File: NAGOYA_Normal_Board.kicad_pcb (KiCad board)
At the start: 2 copper layers, 94 parts, among them CN1 XT30-M, CN13 value, CN14 RefereeSystem, CN15 micro_B, J1 debug, J10 CAN3, J11 CAN3, J12 CAN3, J13 CAN3, J14 CAN3, J15 CAN3, J16 CAN3, J5 CAN3, J6 CAN3, J7 CAN3, J8 CAN3, J9 CAN3, Q2 DDTC114EUA-7-F, U1 Teensy4.1, U10 AP63357, U2 TCAN1042HVDR, U3 TCAN1042HVDR, U4 TCAN1042HVDR, U5 FT234XD, U6 TLP172AM, U7 BNO055, U9 LXES11DAA2-137, Y2 32.768 k

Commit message: PCBwo
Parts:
- removed C15: 47p, Capacitor_SMD:C_0402_1005Metric
- removed C16, C17: 22u, Resistor_SMD:R_1206_3216Metric
- removed D1: LED, LED_SMD:LED_0603_1608Metric
- removed J11, J12, J15, J16: CAN3, Connector_JST:JST_GH_SM02B-GHS-TB_1x02-1MP_P1.25mm_Horizontal
- removed L1: 6.8u, Inductor_SMD:L_TracoPower_TCK-047_5.2x5.8mm
- removed R1: 3.3k, Resistor_SMD:R_0603_1608Metric
- removed R14: 41.2k, Resistor_SMD:R_0201_0603Metric
- removed U10: AP63357, 0_PCB:V-DFN3020-13
- removed ZD12: ESD5Z7.0T1G, Diode_SMD:D_SOD-523
- added CN2: XT30-M, 0_PCB:AMASS_XT30U-M_1x02_P5.0mm_Vertical, F.Cu at (158.8, 90.5)
- added CN3: XT30-F, 0_PCB:AMASS_XT30U-F_1x02_P5.0mm_Vertical, F.Cu at (158.9, 84.0)
- added CN4: XT30-F, 0_PCB:AMASS_XT30U-F_1x02_P5.0mm_Vertical, F.Cu at (158.8, 77.7)
- added CN5: XT30-F, 0_PCB:AMASS_XT30U-F_1x02_P5.0mm_Vertical, F.Cu at (158.9, 71.3)
- added CN6: XT30-F, 0_PCB:AMASS_XT30U-F_1x02_P5.0mm_Vertical, F.Cu at (158.8, 65.0)
- added D6: LED, LED_SMD:LED_0603_1608Metric, F.Cu at (121.4, 123.8)
- added M78AR05-0.5: ~, 0_PCB:SIP3_LMS78-12_GAP, F.Cu at (120.5, 111.6)
- added R5: 3.3k, Resistor_SMD:R_0603_1608Metric, F.Cu at (123.7, 123.0)
- C14: value 0.1u(50V) -> 100uF; footprint Capacitor_SMD:C_0402_1005Metric -> Capacitor_SMD:CP_Elec_6.3x7.7
- CN1: footprint 0_PCB:AMASS_XT30PW-M_1x02_P2.50mm_Horizontal -> 0_PCB:AMASS_XT30U-M_1x02_P5.0mm_Vertical
- R12: value 22k -> 4.7k
- R13: value 220k -> 4.7k; footprint Resistor_SMD:R_0201_0603Metric -> Resistor_SMD:R_0805_2012Metric
- moved U1 232.1 mm to (147.6, 121.4), turned to 180 degrees
- moved J9 215.7 mm to (166.5, 114.5), turned to 90 degrees
- moved H4 214.1 mm to (167.0, 122.0)
- moved J10 210.1 mm to (166.5, 107.4), turned to 90 degrees
- moved H2 205.3 mm to (167.0, 58.0)
- moved C11 203.5 mm to (160.3, 121.8)
- moved C9 203.5 mm to (160.9, 113.1)
- moved D3 203.2 mm to (156.8, 122.4), turned to -90 degrees
- moved D4 201.1 mm to (157.6, 113.2), turned to -90 degrees
- moved C8 200.7 mm to (153.4, 121.6)
- moved J13 199.9 mm to (166.5, 99.9), turned to 90 degrees
- moved J14 195.3 mm to (166.5, 92.8), turned to 90 degrees
- moved C10 193.8 mm to (151.7, 113.5), turned to 180 degrees
- moved CN13 190.2 mm to (154.1, 103.6), turned to 90 degrees
- moved U3 187.3 mm to (153.0, 117.6)
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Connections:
- C13 pad 1: V_BATT -> +5V
- C14 pad 1: Net-(U10-BST) -> +5V
- C14 pad 2: Net-(C14-Pad2) -> GND
- J1 pad 3: RX6 -> RX8
- J1 pad 4: TX6 -> TX8
- J10 pad 1: CAN1_L -> CAN2_L
- J10 pad 2: CAN1_H -> CAN2_H
- J13 pad 1: CAN1_L -> CAN3_L
- J13 pad 2: CAN1_H -> CAN3_H
- J14 pad 1: CAN1_L -> CAN3_L
- J14 pad 2: CAN1_H -> CAN3_H
- J9 pad 1: CAN1_L -> CAN2_L
- J9 pad 2: CAN1_H -> CAN2_H
- JP2 pad 1: VCC -> +3.3V
- JP3 pad 1: VCC -> +3.3V
- R12 pad 1: V_BATT -> +3.3V
- R12 pad 2: GND -> IMU_SCL
- R13 pad 1: +5V -> +3.3V
- R13 pad 2: Net-(U10-FB) -> IMU_SDA
- R3 pad 1: CAN1_L -> CAN2_L
- R3 pad 2: CAN1_H -> CAN2_H
- R4 pad 1: CAN1_L -> CAN3_L
- R4 pad 2: CAN1_H -> CAN3_H
- U3 pad 6: CAN1_L -> CAN2_L
- U3 pad 7: CAN1_H -> CAN2_H
- U4 pad 6: CAN1_L -> CAN3_L
- U4 pad 7: CAN1_H -> CAN3_H
- ZD4 pad 1: CAN1_H -> CAN2_H
- ZD4 pad 2: CAN1_L -> CAN2_L
- ZD5 pad 1: CAN1_H -> CAN3_H
- ZD5 pad 2: CAN1_L -> CAN3_L
- ZD8 pad 1: TX6 -> TX8
- ZD9 pad 1: RX6 -> RX8
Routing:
- net +5V: track 0.00 -> 142.8 mm, vias 0 -> 6
- net +3.3V: track 0.00 -> 118.7 mm, vias 0 -> 7
- net CAN1_L: track 0.00 -> 52.6 mm, vias 0 -> 4
- net IMU_SDA: track 0.00 -> 52.5 mm, vias 0 -> 2
- net IMU_SCL: track 0.00 -> 51.8 mm, vias 0 -> 2
- net CAN_RX3: track 0.00 -> 50.7 mm, vias 0 -> 1
- net CAN_TX3: track 0.00 -> 48.4 mm, vias 0 -> 1
- net CAN1_H: track 0.00 -> 47.1 mm, vias 0 -> 4
- net CAN_RX1: track 0.00 -> 27.6 mm, vias 0 -> 2
- net CAN3_L: track 0.00 -> 26.9 mm
- net CAN_TX1: track 0.00 -> 26.6 mm, vias 0 -> 1
- net CAN3_H: track 0.00 -> 26.1 mm
- net RX3: track 0.00 -> 24.9 mm, vias 0 -> 2
- net TX3: track 0.00 -> 23.4 mm, vias 0 -> 2
- net Controller_RX: track 0.00 -> 22.8 mm
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- added copper zone on B.Cu, net Ammo_GND
- added copper zone on F.Cu, net Ammo_GND
- added copper zone on B.Cu, net GND
- added copper zone on F.Cu, net GND
- added copper zone on B.Cu, net V_Ammo
- added copper zone on F.Cu, net V_Ammo
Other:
- board outline added: 60 x 70 mm

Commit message: Update
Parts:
- added D10: LED, LED_SMD:LED_0603_1608Metric, F.Cu at (125.4, 80.5)
- added D8: LED, LED_SMD:LED_0603_1608Metric, F.Cu at (125.3, 76.8)
- added D9: LED, LED_SMD:LED_0603_1608Metric, F.Cu at (125.4, 78.8)
- added G***: LOGO, LOGO, F.Cu at (159.4, 58.6)
- added G***: LOGO, LOGO, F.Cu at (143.2, 118.0)
- added G***: LOGO, LOGO, F.Cu at (140.6, 85.4)
- added Q4: DDTC114EUA-7-F, Package_TO_SOT_SMD:SOT-323_SC-70, F.Cu at (129.0, 76.2)
- added Q5: DDTC114EUA-7-F, Package_TO_SOT_SMD:SOT-323_SC-70, F.Cu at (129.0, 78.8)
- added Q6: DDTC114EUA-7-F, Package_TO_SOT_SMD:SOT-323_SC-70, F.Cu at (129.0, 81.3)
- added R14: 3.3k, Resistor_SMD:R_0603_1608Metric, F.Cu at (122.0, 78.7)
- added R16: 3.3k, Resistor_SMD:R_0603_1608Metric, F.Cu at (122.1, 80.5)
- added R7: 3.3k, Resistor_SMD:R_0603_1608Metric, F.Cu at (122.1, 76.8)
- moved C7 10.5 mm to (119.1, 89.3), turned to 180 degrees
- moved R2 9.69 mm to (118.0, 85.4), turned to -90 degrees
- moved C6 7.99 mm to (125.0, 91.5), turned to -90 degrees
- moved D2 7.70 mm to (122.3, 89.2)
- moved ZD3 4.91 mm to (121.2, 85.3), turned to 180 degrees
- moved U2 3.96 mm to (127.0, 85.3), turned to 180 degrees
- moved CN3 3.50 mm to (162.4, 84.0)
- moved CN4 3.50 mm to (162.3, 77.7)
- moved CN5 3.50 mm to (162.4, 71.3)
- moved CN6 3.50 mm to (162.3, 65.0)
- moved C1 2.19 mm to (145.0, 84.0), turned to -90 degrees
- moved R13 1.39 mm to (138.3, 100.0)
- moved C4 1.29 mm to (122.8, 96.7)
- moved H2 1.00 mm to (167.0, 57.0)
- moved H3 1.00 mm to (113.0, 57.0)
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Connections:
- C22 pad 2: GNDA -> GND
- C23 pad 1: GNDA -> GND
- C24 pad 1: GNDA -> GND
- C26 pad 2: GNDA -> Net-(ZD11-A)
- JP1 pad 2: GNDA -> GND
- R48 pad 1: GNDA -> GND
- R49 pad 1: GNDA -> GND
- U1 pad 30: unconnected-(U1-38-Pad30) -> LED2
- U1 pad 31: unconnected-(U1-39-Pad31) -> LED3
- U1 pad 32: unconnected-(U1-40-Pad32) -> LED4
- U7 pad 15: GNDA -> GND
- U7 pad 16: GNDA -> GND
- U7 pad 17: GNDA -> GND
- U7 pad 2: GNDA -> GND
- U7 pad 25: GNDA -> GND
- ZD11 pad 2: GNDA -> Net-(ZD11-A)
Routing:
- net +3.3V: track 118.7 -> 188.4 mm, vias 7 -> 10
- net +5V: track 142.8 -> 186.2 mm, vias 6 -> 4
- net CAN1_L: track 52.6 -> 31.1 mm, vias 4 -> 2
- net GND: track 5.19 -> 17.8 mm, vias 3 -> 5
- net CAN1_H: track 47.1 -> 38.4 mm, vias 4 -> 0
- net CAN_RX1: track 27.6 -> 35.7 mm, vias 2 -> 1
- net /Vio: track 14.2 -> 21.0 mm
- net Net-(U5-3V3OUT): track 1.44 -> 5.50 mm, vias 0 -> 1
- net UART4_RX: track 4.00 -> 0.58 mm
- net UART4_TX: track 4.02 -> 0.65 mm, vias 1 -> 0
- net LED4: track 0.00 -> 2.90 mm
- net LED3: track 0.00 -> 2.87 mm
- net LED2: track 0.00 -> 2.85 mm
- net CAN_TX1: track 26.6 -> 29.1 mm
- net Net-(D10-K): track 0.00 -> 2.15 mm
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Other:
- board size 60 x 70 mm -> 60 x 71 mm

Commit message: recommit
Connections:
- C11 pad 1: /Vio -> Net-(D4-K)
- C7 pad 1: /Vio -> Net-(D2-K)
- C9 pad 1: /Vio -> Net-(D3-K)
- D2 pad 1: /Vio -> Net-(D2-K)
- D3 pad 1: /Vio -> Net-(D3-K)
- D4 pad 1: /Vio -> Net-(D4-K)
- U2 pad 5: /Vio -> Net-(D2-K)
- U3 pad 5: /Vio -> Net-(D3-K)
- U4 pad 5: /Vio -> Net-(D4-K)
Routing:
- net /Vio: track 21.0 -> 0.00 mm
- net Net-(D2-K): track 0.00 -> 11.5 mm
- net (no net): track 0.00 -> 9.50 mm

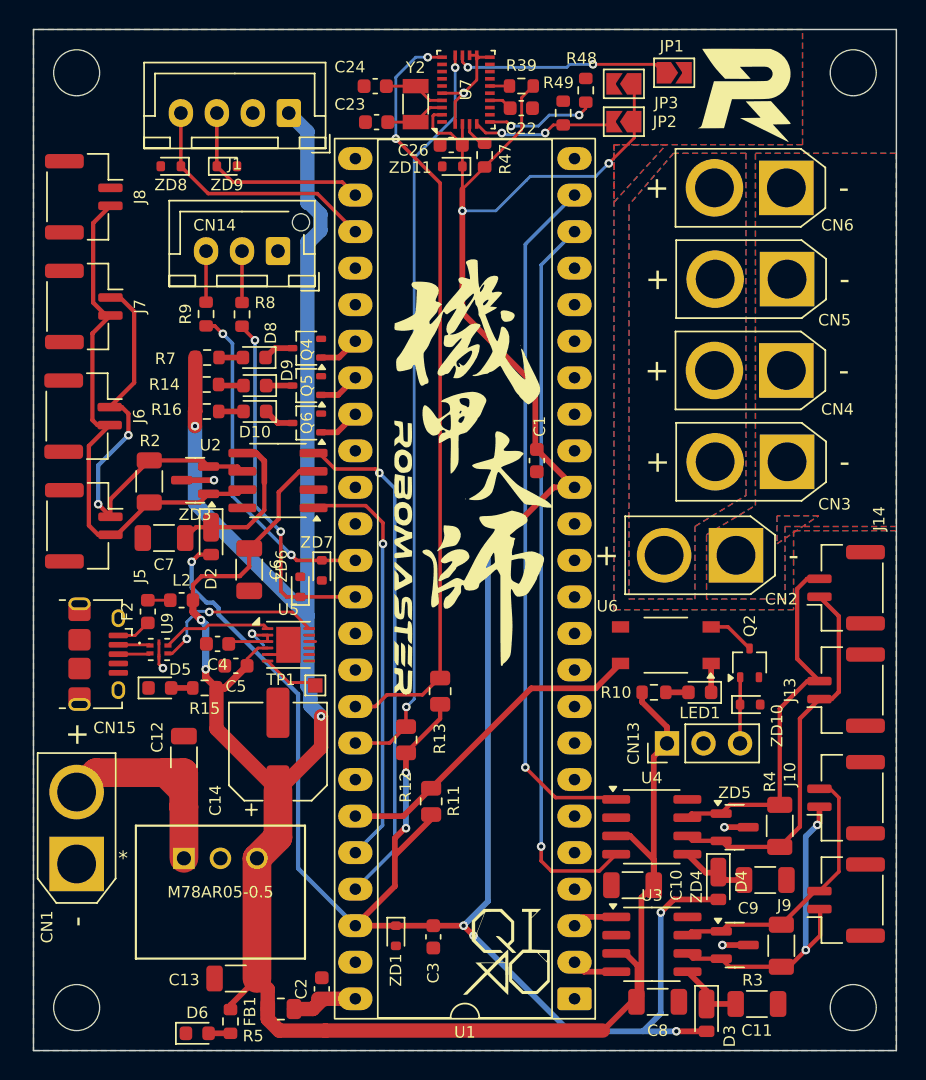
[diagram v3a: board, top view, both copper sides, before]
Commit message: USBシリアルを絶縁＞パターン変更
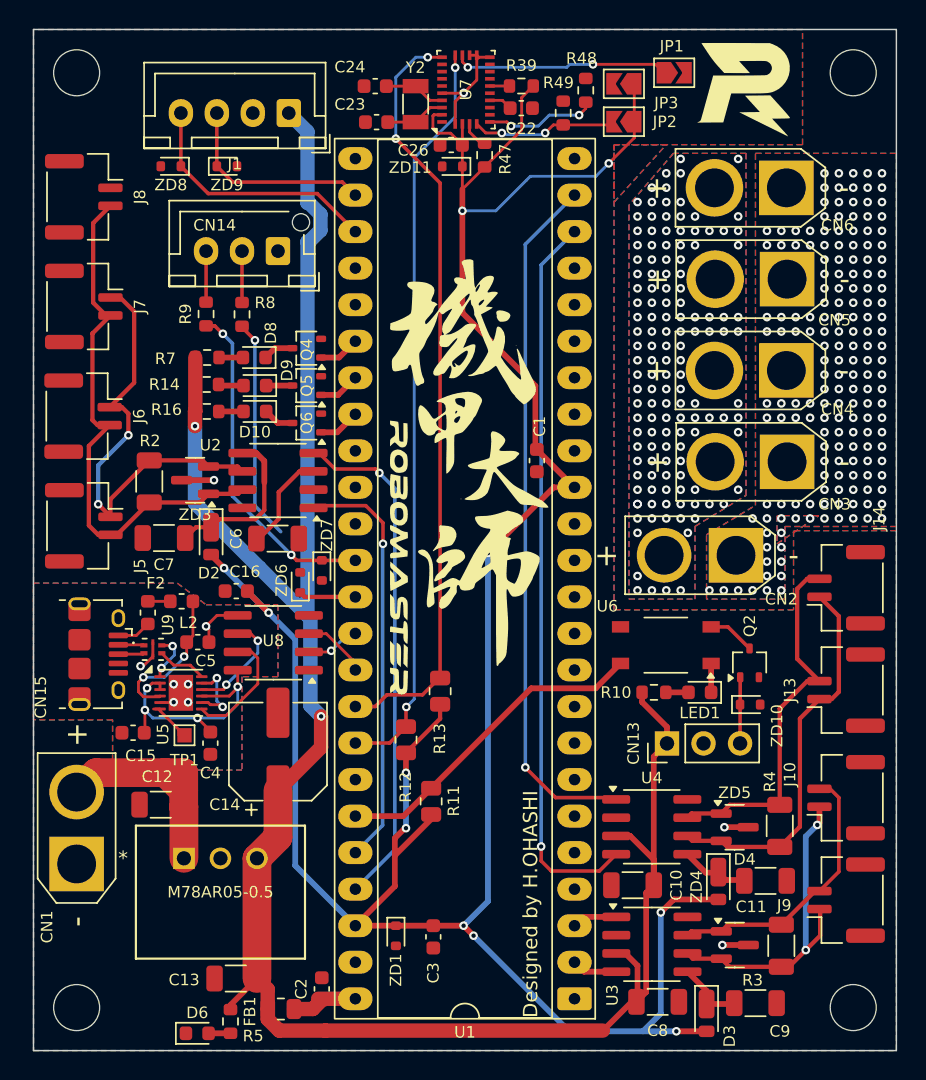
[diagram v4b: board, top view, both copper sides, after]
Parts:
- removed D5: LED, LED_SMD:LED_0603_1608Metric
- removed the G*** at (143.2, 118.0)
- removed R15: 1k, Resistor_SMD:R_0603_1608Metric
- added C15: 0.1u, Capacitor_SMD:C_0603_1608Metric, F.Cu at (116.9, 102.9)
- added C16: 0.1u, Capacitor_SMD:C_0603_1608Metric, F.Cu at (124.1, 93.0)
- added U8: ADuM121N, Package_SO:SOIC-8_3.9x4.9mm_P1.27mm, F.Cu at (126.7, 96.6)
- moved TP1 9.74 mm to (120.5, 103.1)
- moved C9 8.59 mm to (160.2, 121.7)
- moved C11 8.58 mm to (160.9, 113.2)
- moved U5 8.19 mm to (120.2, 100.1)
- moved C4 6.92 mm to (122.3, 103.6), turned to -90 degrees
- moved C12 3.66 mm to (118.8, 107.9), turned to 180 degrees
- moved C5 3.12 mm to (121.4, 96.6), turned to 0 degrees
- moved C6 2.93 mm to (127.0, 89.4), turned to 0 degrees
- moved U9 0.43 mm to (118.3, 97.1)
- moved G*** 0.40 mm to (159.3, 58.2)
- moved ZD6 0.31 mm to (128.6, 92.4)
- moved G*** 0.30 mm to (140.3, 85.4)
- moved F2 0.08 mm to (118.0, 94.5)
- moved L2 0.08 mm to (120.3, 93.8)
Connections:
- C4 pad 2: GND -> GNDREF
- C5 pad 1: +5V -> Net-(U5-VCC)
- C5 pad 2: GND -> GNDREF
- CN15 pad 5: GND -> GNDREF
- CN15 pad 6: GND -> GNDREF
- L2 pad 1: +5V -> Net-(U5-VCC)
- U5 pad 10: UART4_TX -> Net-(U5-RXD/D1)
- U5 pad 13: GND -> GNDREF
- U5 pad 4: +5V -> Net-(U5-VCC)
- U5 pad 5: GND -> GNDREF
- U5 pad 7: UART4_RX -> Net-(U5-TXD/D0)
- U9 pad 3: GND -> GNDREF
- U9 pad 6: GND -> GNDREF
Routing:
- net +5V: track 186.2 -> 157.8 mm, vias 4 -> 2
- net Net-(U5-3V3OUT): track 5.50 -> 18.3 mm, vias 1 -> 4
- net Net-(U5-VCC): track 0.00 -> 10.4 mm, vias 0 -> 2
- net (no net): track 9.50 -> 0.00 mm
- net Net-(U5-USBDP): track 12.2 -> 3.45 mm, vias 2 -> 0
- net Net-(U5-TXD/D0): track 0.00 -> 8.37 mm
- net GNDREF: track 0.00 -> 7.56 mm, vias 0 -> 6
- net Net-(U5-RXD/D1): track 0.00 -> 7.50 mm, vias 0 -> 2
- net RX3: track 24.9 -> 19.4 mm, vias 2 -> 1
- net Net-(U5-~{CTS}/D3): track 0.00 -> 4.95 mm, vias 0 -> 2
- net Net-(D3-K): track 0.00 -> 4.82 mm
- net Net-(D4-K): track 0.00 -> 4.68 mm
- net UART4_RX: track 0.58 -> 5.00 mm, vias 0 -> 1
- net Net-(U5-USBDM): track 7.62 -> 3.36 mm, vias 0 -> 2
- net UART4_TX: track 0.65 -> 4.77 mm
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- added copper zone on B.Cu, net GNDREF
- added copper zone on F.Cu, net GNDREF
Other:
- board text added: "Designed by H.OHASHI"

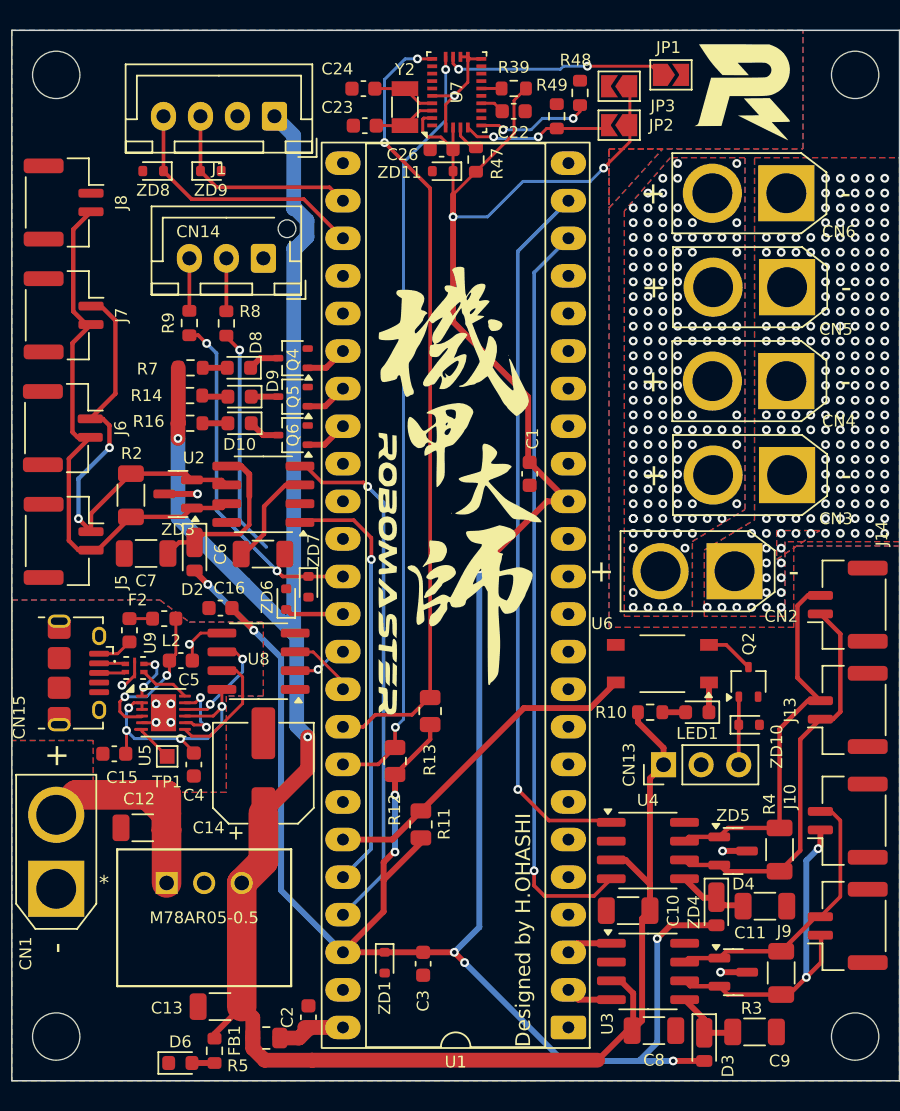
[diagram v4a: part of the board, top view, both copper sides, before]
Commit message: USBシリアルを絶縁
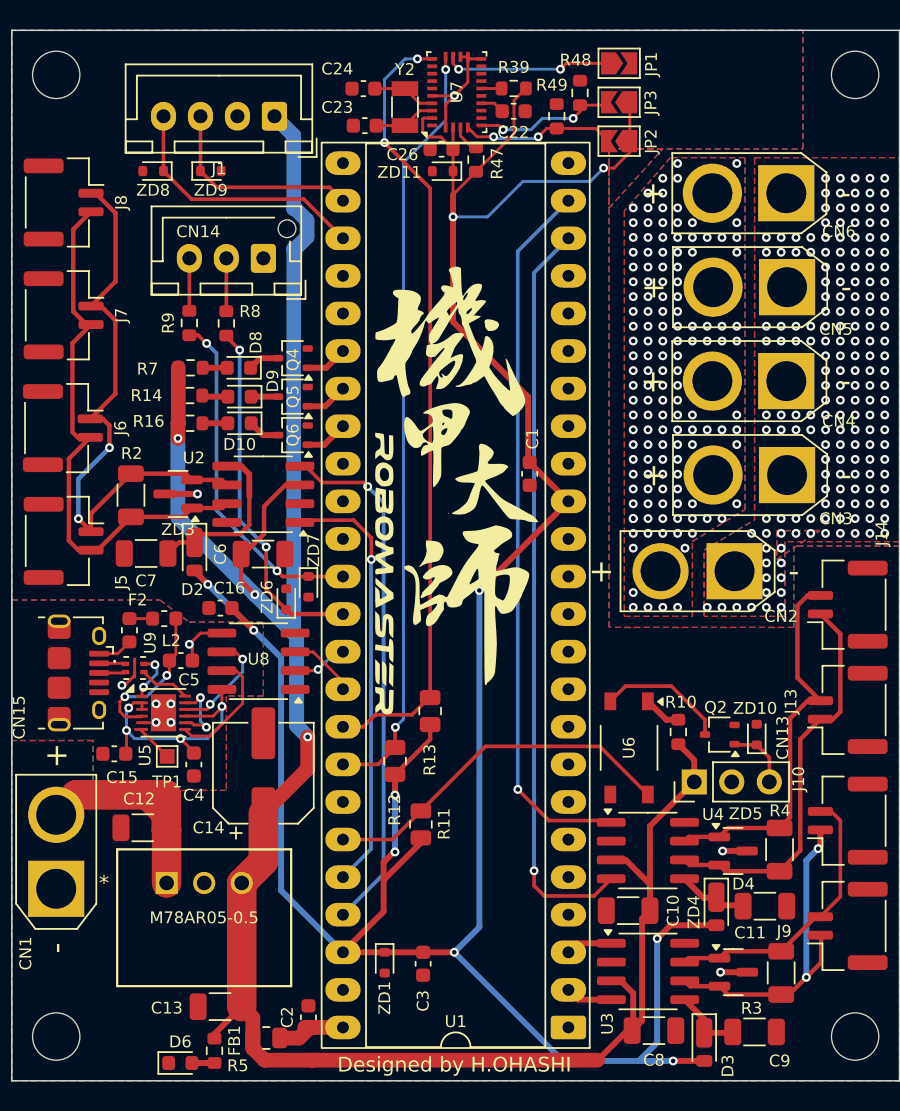
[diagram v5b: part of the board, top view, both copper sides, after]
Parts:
- removed the G*** at (159.3, 58.2)
- removed LED1: RED, LED_SMD:LED_0603_1608Metric
- moved U6 6.12 mm to (151.7, 102.5), turned to -90 degrees
- moved Q2 4.05 mm to (157.8, 101.6), turned to 180 degrees
- moved JP1 3.59 mm to (151.1, 56.2)
- moved CN13 2.37 mm to (156.1, 104.8)
- moved R10 2.33 mm to (155.1, 101.4), turned to 90 degrees
- moved JP2 1.08 mm to (151.0, 61.5)
- moved JP3 1.08 mm to (151.0, 58.9)
- moved ZD10 0.84 mm to (160.3, 101.6), turned to 90 degrees
- moved G*** 0.23 mm to (140.1, 85.4)
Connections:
- R10 pad 2: Net-(LED1-A) -> Net-(R10-Pad2)
- U6 pad 1: Net-(LED1-K) -> Net-(R10-Pad2)
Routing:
- net CAN1_L: track 31.1 -> 40.3 mm
- net Net-(Q2-C): track 3.29 -> 8.77 mm
- net RX3: track 19.4 -> 24.1 mm, vias 1 -> 2
- net Net-(JP1-A): track 14.9 -> 11.3 mm
- net Net-(R10-Pad2): track 0.00 -> 2.58 mm
- net Net-(LED1-K): track 2.28 -> 0.00 mm
- net Net-(JP3-B): track 7.73 -> 9.73 mm
- net Controller_RX: track 22.8 -> 24.6 mm
- net Net-(LED1-A): track 1.57 -> 0.00 mm
- net +5V: track 157.8 -> 159.3 mm, vias 2 -> 3
- net +3.3V: track 188.6 -> 187.1 mm, vias 11 -> 10

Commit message: 発注用データ
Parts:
- added R50: 10k, Resistor_SMD:R_0603_1608Metric, F.Cu at (150.7, 91.7)
- added R51: 10k, Resistor_SMD:R_0603_1608Metric, F.Cu at (152.2, 91.7)
- added R52: 10k, Resistor_SMD:R_0603_1608Metric, F.Cu at (153.7, 91.7)
- added R53: 10k, Resistor_SMD:R_0603_1608Metric, F.Cu at (155.2, 91.7)
- added SW1: SW_DIP_x04, Button_Switch_SMD:SW_DIP_SPSTx04_Slide_Copal_CHS-04A_W5.08mm_P1.27mm_JPin, F.Cu at (159.6, 95.9)
- moved CN2 5.01 mm to (162.4, 87.0)
- moved CN4 3.51 mm to (162.3, 74.2)
- moved CN6 3.51 mm to (162.3, 61.5)
- moved CN3 3.51 mm to (162.4, 80.5)
- moved CN5 3.51 mm to (162.4, 67.8)
- moved J13 1.06 mm to (166.5, 101.0)
- moved J14 1.06 mm to (166.5, 93.9)
- moved J10 0.81 mm to (166.5, 108.2)
- moved J9 0.80 mm to (166.5, 115.3)
- moved C26 0.68 mm to (139.0, 62.7)
- moved R47 0.68 mm to (141.4, 63.4)
- moved ZD11 0.68 mm to (139.1, 64.2)
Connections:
- U1 pad 11: unconnected-(U1-9-Pad11) -> DIP_SW_4
- U1 pad 12: unconnected-(U1-10-Pad12) -> DIP_SW_3
- U1 pad 13: unconnected-(U1-11-Pad13) -> DIP_SW_2
- U1 pad 14: unconnected-(U1-12-Pad14) -> DIP_SW_1
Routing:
- net GND: track 14.1 -> 55.3 mm, vias 4 -> 334
- net +3.3V: track 187.1 -> 206.1 mm
- net DIP_SW_1: track 0.00 -> 18.4 mm
- net DIP_SW_2: track 0.00 -> 16.8 mm, vias 0 -> 1
- net DIP_SW_3: track 0.00 -> 14.4 mm, vias 0 -> 1
- net DIP_SW_4: track 0.00 -> 13.4 mm, vias 0 -> 1
- net CAN2_L: track 22.7 -> 20.5 mm
- net Net-(ZD11-A): track 0.00 -> 1.55 mm
- net CAN3_H: track 25.9 -> 25.0 mm
- net CAN2_H: track 19.7 -> 18.7 mm
- net CAN3_L: track 26.9 -> 26.0 mm
- net Net-(U7-~{BOOT_LOAD_PIN}): track 1.94 -> 2.46 mm
- net GNDREF: track 7.56 -> 7.16 mm, vias 6 -> 31
- net V_Ammo: vias 136 -> 168
- net Ammo_GND: vias 172 -> 203
